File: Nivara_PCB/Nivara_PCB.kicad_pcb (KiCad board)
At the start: 2 copper layers, 102.2 x 83 mm, 58 parts, among them J1 NPN_IN, J10 Analog_Out, J11 RELAY, J2 PNP_IN, J3 D_IN, J4 Analaog_In, J5 RUN/STOP, J6 FUENTE, J7 NPN_OUT, J8 PNP_OUT, J9 RS485, Q1 IRLML6344, Q2 IRLML6344, Q3 IRLML6402, Q4 IRLML6402, U1 ESP32-S3-WROOM-1, U2 AP63203WU, U3 AP63205WU

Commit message: Cambios en el RS485
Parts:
- moved U1 17.7 mm to (194.1, 102.8)
- moved R5 9.10 mm to (155.7, 68.4), turned to 90 degrees
- renumbered TP4 to TP2, TP2 to TP3, TP3 to TP4
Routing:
- net /NIVARA_BOARD/NPN_IN/ESP_NPN_IN_1: track 8.14 -> 2.72 mm
- net +3.3V: track 82.8 -> 80.6 mm, vias 2 -> 4
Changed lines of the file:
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@@
 		(descr "SMD rectangular pad as test Point, square 1.0mm side length")
 		(tags "test point SMD pad rectangle square")
-		(property "Reference" "TP3"
+		(property "Reference" "TP4"
 			(at 0 -1.448 0)
 			(layer "F.SilkS")
@@
 	(footprint "RF_Module:ESP32-S3-WROOM-1"
 		(layer "F.Cu")
-		(at 184.7 87.75 -90)
+		(at 194.1 102.8 -90)
 		(descr "2.4 GHz Wi-Fi and Bluetooth module  https://www.espressif.com/sites/default/files/documentation/esp32-s3-wroom-1_wroom-1u_datasheet_en.pdf")
 		(tags "2.4 GHz Wi-Fi and Bluetooth module")
@@
 			(polygon
 				(pts
-					(xy 191.45 63.75) (xy 191.45 111.75) (xy 212.45 111.75) (xy 212.45 63.75)
+					(xy 200.85 78.8) (xy 200.85 126.8) (xy 221.85 126.8) (xy 221.85 78.8)
 				)
 			)
@@
 		(descr "SMD rectangular pad as test Point, square 1.0mm side length")
 		(tags "test point SMD pad rectangle square")
-		(property "Reference" "TP4"
+		(property "Reference" "TP2"
 			(at 0 -1.448 0)
 			(layer "F.SilkS")
@@
 		(descr "SMD rectangular pad as test Point, square 1.0mm side length")
 		(tags "test point SMD pad rectangle square")
-		(property "Reference" "TP2"
+		(property "Reference" "TP3"
 			(at 2.5 -0.1 0)
 			(layer "F.SilkS")
@@
 	(footprint "PCM_Resistor_SMD_AKL:R_0603_1608Metric"
 		(layer "F.Cu")
-		(at 164.7 69.7)
+		(at 155.7 68.375 90)
 		(descr "Resistor SMD 0603 (1608 Metric), square (rectangular) end terminal, IPC_7351 nominal, (Body size source: IPC-SM-782 page 72, https://www.pcb-3d.com/wordpress/wp-content/uploads/ipc-sm-782a_amendment_1_and_2.pdf), Alternate KiCad Library")
 		(tags "resistor")
 		(property "Reference" "R5"
-			(at -3.175 0 0)
+			(at -3.175 0 90)
 			(layer "F.SilkS")
 			(effects
@@
 		)
 		(property "Value" "10k"
-			(at 0 1.43 0)
+			(at 0 1.43 90)
 			(layer "F.Fab")
 			(hide yes)
@@
 		)
 		(property "Datasheet" ""
-			(at 0 0 0)
+			(at 0 0 90)
 			(layer "F.Fab")
 			(hide yes)
@@
 		)
 		(property "Description" "SMD 0603 Chip Resistor, US Symbol, Alternate KiCad Library"
-			(at 0 0 0)
+			(at 0 0 90)
 			(layer "F.Fab")
 			(hide yes)
@@
 		(attr smd)
 		(fp_line
-			(start -1.5 -0.8)
-			(end -1.5 0.8)
+			(start 1.5 -0.8)
+			(end -1.5 -0.8)
 			(stroke
 				(width 0.12)
@@
 		)
 		(fp_line
-			(start -1.5 0.8)
-			(end 1.5 0.8)
+			(start -1.5 -0.8)
+			(end -1.5 0.8)
 			(stroke
 				(width 0.12)
@@
 		)
 		(fp_line
-			(start 1.5 -0.8)
-			(end -1.5 -0.8)
+			(start 1.5 0.8)
+			(end 1.5 -0.8)
 			(stroke
 				(width 0.12)
@@
 		)
 		(fp_line
-			(start 1.5 0.8)
-			(end 1.5 -0.8)
+			(start -1.5 0.8)
+			(end 1.5 0.8)
 			(stroke
 				(width 0.12)
@@
 		)
 		(fp_line
-			(start -1.48 -0.73)
-			(end 1.48 -0.73)
+			(start 1.48 -0.73)
+			(end 1.48 0.73)
 			(stroke
 				(width 0.05)
@@
 		)
 		(fp_line
-			(start -1.48 0.73)
-			(end -1.48 -0.73)
+			(start -1.48 -0.73)
+			(end 1.48 -0.73)
 			(stroke
 				(width 0.05)
@@
 		)
 		(fp_line
-			(start 1.48 -0.73)
-			(end 1.48 0.73)
+			(start 1.48 0.73)
+			(end -1.48 0.73)
 			(stroke
 				(width 0.05)
@@
 		)
 		(fp_line
-			(start 1.48 0.73)
-			(end -1.48 0.73)
+			(start -1.48 0.73)
+			(end -1.48 -0.73)
 			(stroke
 				(width 0.05)
@@
 		)
 		(fp_line
-			(start -0.8 -0.4125)
-			(end 0.8 -0.4125)
+			(start 0.8 -0.4125)
+			(end 0.8 0.4125)
 			(stroke
 				(width 0.1)
@@
 		)
 		(fp_line
-			(start -0.8 0.4125)
-			(end -0.8 -0.4125)
+			(start -0.8 -0.4125)
+			(end 0.8 -0.4125)
 			(stroke
 				(width 0.1)
@@
 		)
 		(fp_line
-			(start 0.8 -0.4125)
-			(end 0.8 0.4125)
+			(start 0.8 0.4125)
+			(end -0.8 0.4125)
 			(stroke
 				(width 0.1)
@@
 		)
 		(fp_line
-			(start 0.8 0.4125)
-			(end -0.8 0.4125)
+			(start -0.8 0.4125)
+			(end -0.8 -0.4125)
 			(stroke
 				(width 0.1)
@@
 		)
 		(fp_text user "${REFERENCE}"
-			(at 0 0 0)
+			(at 0 0 90)
 			(layer "F.Fab")
 			(effects
@@
 		)
 		(pad "1" smd roundrect
-			(at -0.825 0)
+			(at -0.825 0 90)
 			(size 0.8 0.95)
 			(layers "F.Cu" "F.Mask" "F.Paste")
@@
 		)
 		(pad "2" smd roundrect
-			(at 0.825 0)
+			(at 0.825 0 90)
 			(size 0.8 0.95)
 			(layers "F.Cu" "F.Mask" "F.Paste")
@@
 	)
 	(segment
-		(start 153.45 69.7)
+		(start 152.95 69.2)
 		(end 151.65 67.9)
 		(width 0.4)
@@
 	)
 	(segment
-		(start 108.2 64.05)
-		(end 107.1 62.95)
-		(width 0.6)
+		(start 155.7 69.2)
+		(end 152.95 69.2)
+		(width 0.4)
 		(layer "F.Cu")
 		(net 1)
 	)
 	(segment
-		(start 169.2 68)
-		(end 169.2 67.525)
-		(width 0.4)
+		(start 108.2 64.05)
+		(end 107.1 62.95)
+		(width 0.6)
 		(layer "F.Cu")
 		(net 1)
@@
 	)
 	(segment
-		(start 163.875 69.7)
-		(end 153.45 69.7)
-		(width 0.4)
-		(layer "F.Cu")
-		(net 1)
-	)
-	(segment
 		(start 108.2 64.95)
 		(end 108.2 64.05)
@@
 	)
 	(segment
-		(start 166.1 71.1)
-		(end 169.2 68)
-		(width 0.4)
-		(layer "F.Cu")
-		(net 1)
-	)
-	(segment
 		(start 106.15 64.95)
 		(end 110.5 64.95)
@@
 	)
 	(segment
-		(start 164.6 71.1)
-		(end 166.1 71.1)
-		(width 0.4)
-		(layer "F.Cu")
-		(net 1)
-	)
-	(segment
-		(start 163.875 70.375)
-		(end 164.6 71.1)
-		(width 0.4)
-		(layer "F.Cu")
-		(net 1)
-	)
-	(segment
 		(start 105.9 72.1)
 		(end 106.05 71.95)
@@
 		(net 1)
 	)
-	(segment
-		(start 163.875 69.7)
-		(end 163.875 70.375)
-		(width 0.4)
-		(layer "F.Cu")
-		(net 1)
-	)
 	(via
 		(at 149.825 67.9)
@@
 		(net 1)
 	)
+	(via
+		(at 169.2 67.525)
+		(size 0.6)
+		(drill 0.3)
+		(layers "F.Cu" "B.Cu")
+		(net 1)
+	)
+	(via
+		(at 155.7 69.2)
+		(size 0.6)
+		(drill 0.3)
+		(layers "F.Cu" "B.Cu")
+		(net 1)
+	)
 	(segment
 		(start 140.2 67.9)
@@
 	)
 	(segment
+		(start 167.525 69.2)
+		(end 169.2 67.525)
+		(width 0.4)
+		(layer "B.Cu")
+		(net 1)
+	)
+	(segment
+		(start 155.7 69.2)
+		(end 167.525 69.2)
+		(width 0.4)
+		(layer "B.Cu")
+		(net 1)
+	)
+	(segment
 		(start 149.825 67.9)
 		(end 140.2 67.9)
@@
 	)
 	(via
-		(at 166.1 68.4)
+		(at 166.9 67.8)
 		(size 0.6)
 		(drill 0.3)
@@
 	)
 	(segment
-		(start 164.225 68.4)
-		(end 159.38 68.4)
-		(width 0.4)
-		(layer "F.Cu")
-		(net 74)
-	)
-	(segment
-		(start 165.525 69.7)
-		(end 164.225 68.4)
+		(start 158.17 67.55)
+		(end 158.35 67.37)
 		(width 0.4)
 		(layer "F.Cu")
@@
 	)
 	(segment
-		(start 159.38 68.4)
-		(end 158.35 67.37)
+		(start 155.7 67.55)
+		(end 158.17 67.55)
 		(width 0.4)
 		(layer "F.Cu")

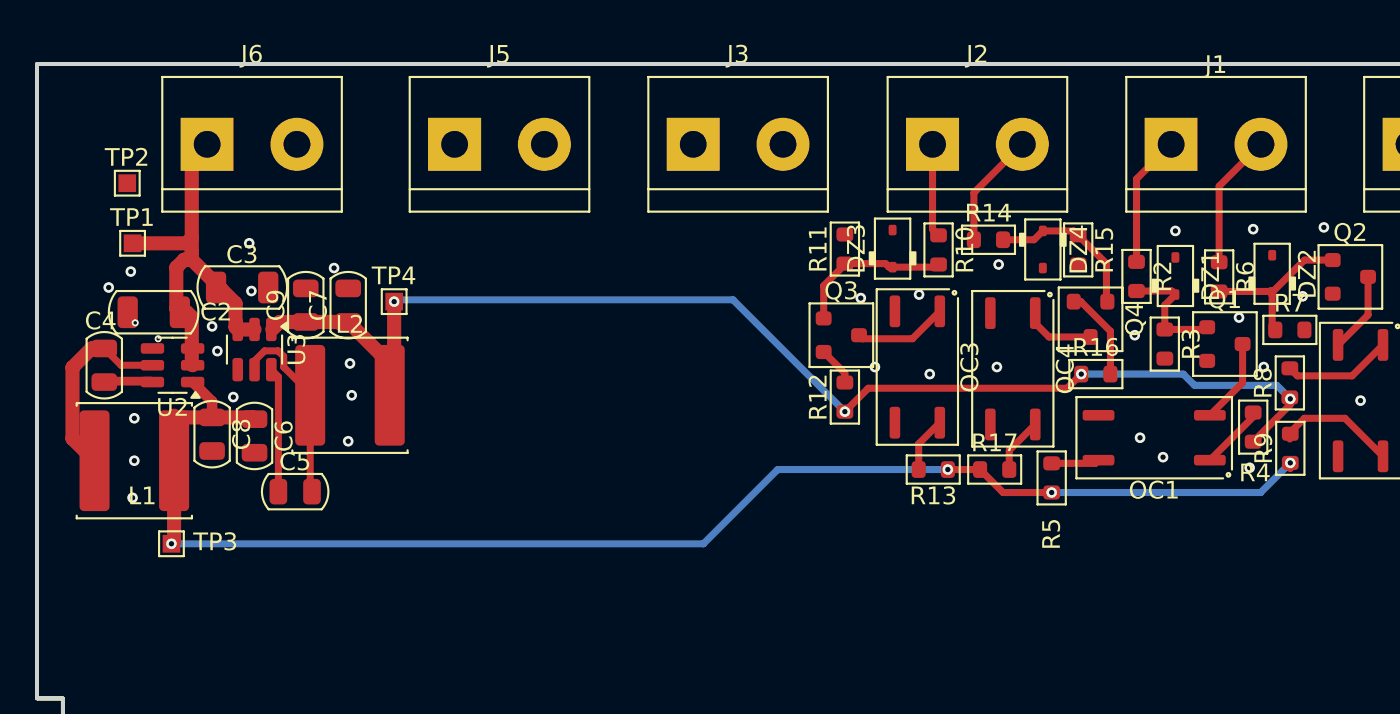
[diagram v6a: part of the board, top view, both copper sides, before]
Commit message: Añadido de diodo TVS y resetteable fuse.
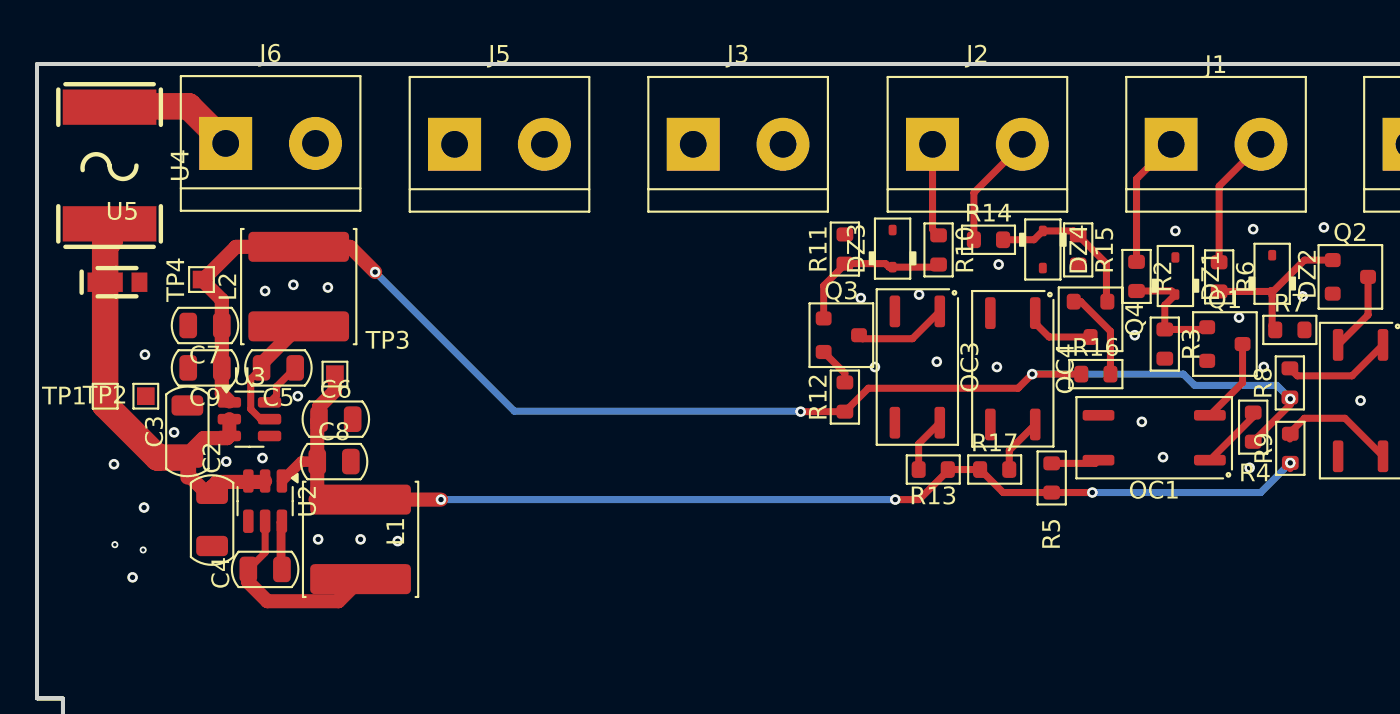
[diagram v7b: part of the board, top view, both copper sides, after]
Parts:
- added U4: 2920L185DR, Fuse_Holder:F2920, F.Cu at (102.4, 50.7)
- added U5: CUHZ30V,H3F, Fuse_Holder:SOD-323HE_L2.0-W1.4-LS2.5-RD, F.Cu at (103.1, 57.3)
- moved C4 14.7 mm to (111.2, 73.5), turned to 180 degrees
- moved L1 13.6 mm to (116.6, 71.8), turned to 90 degrees
- moved TP3 13.3 mm to (115.2, 62.5), turned to 90 degrees
- moved C2 12.2 mm to (108.2, 70.8), turned to -90 degrees
- moved TP2 12.1 mm to (104.5, 63.8), turned to 90 degrees
- moved TP4 11.0 mm to (107.6, 57.1), turned to 90 degrees
- moved U2 9.30 mm to (111.2, 69.7), turned to -90 degrees
- moved TP1 8.79 mm to (102.2, 63.8), turned to 90 degrees
- moved C3 8.72 mm to (106.8, 65.8), turned to 90 degrees
- moved C7 8.18 mm to (107.8, 59.8), turned to 180 degrees
- moved C8 7.07 mm to (115.1, 67.5), turned to 0 degrees
- moved C5 7.06 mm to (112.0, 62.1), turned to 180 degrees
- moved L2 6.80 mm to (113.1, 57.5), turned to 90 degrees
- moved C9 6.72 mm to (107.8, 62.1), turned to 180 degrees
- moved C6 4.70 mm to (115.2, 65.0), turned to 0 degrees
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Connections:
- J6 pad 1: VCC -> Net-(J6-Pin_1)
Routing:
- net +3.3V: track 80.6 -> 67.1 mm
- net +5V: track 73.1 -> 81.3 mm
- net Net-(J6-Pin_1): track 0.00 -> 7.46 mm
- net Net-(U3-BST): track 7.07 -> 2.55 mm
- net VCC: track 23.5 -> 27.6 mm
- net Net-(U3-SW): track 10.8 -> 7.10 mm

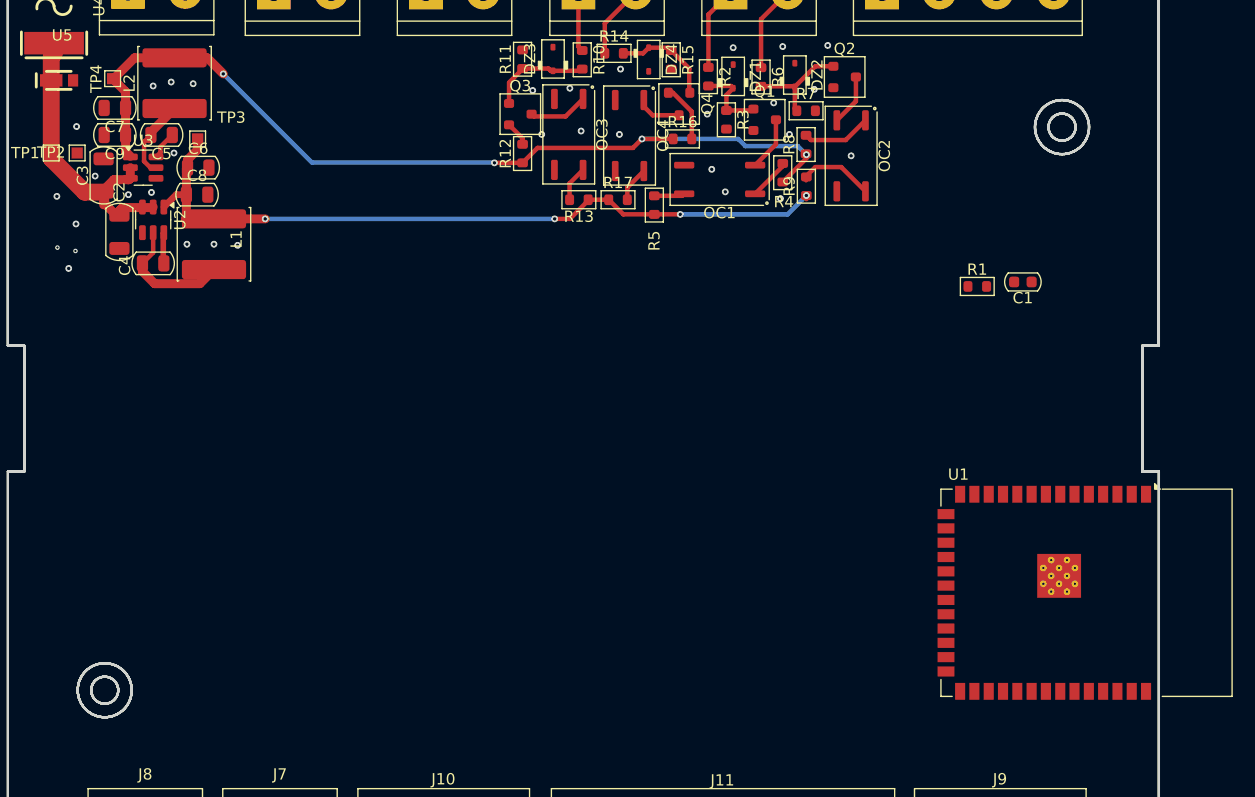
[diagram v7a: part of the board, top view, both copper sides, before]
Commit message: Ajuste de RS-485 y protección de alimentación contra cortocircuito y sobre voltaje.
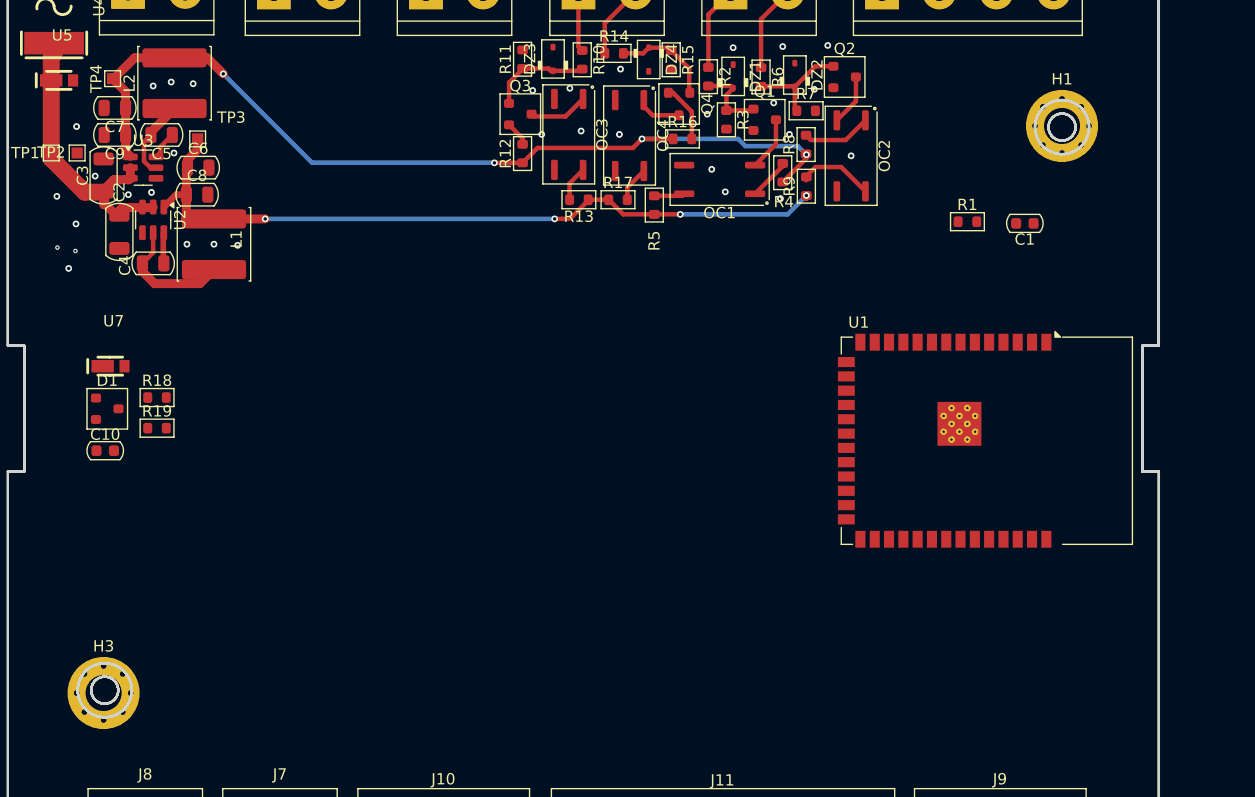
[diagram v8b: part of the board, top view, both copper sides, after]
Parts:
- added C10: 1uF, PCM_Capacitor_SMD_AKL:C_0603_1608Metric, F.Cu at (106.9, 90.2)
- added D1: SM712, PCM_Package_TO_SOT_SMD_AKL:SOT-23, F.Cu at (107.1, 86.5)
- added H1: MountingHole_Pad, MountingHole:MountingHole_3.2mm_M3_Pad_Via, F.Cu at (191.9, 61.4)
- added H3: MountingHole_Pad, MountingHole:MountingHole_3.2mm_M3_Pad_Via, F.Cu at (106.8, 111.7)
- added R18: R_0603, PCM_Resistor_SMD_AKL:R_0603_1608Metric, F.Cu at (111.5, 85.5)
- added R19: R_0603, PCM_Resistor_SMD_AKL:R_0603_1608Metric, F.Cu at (111.5, 88.2)
- added U7: CUHZ30V,H3F, Fuse_Holder:SOD-323HE_L2.0-W1.4-LS2.5-RD, F.Cu at (107.7, 82.7)
- moved U1 16.1 mm to (185.2, 89.3)
- moved R1 5.82 mm to (183.5, 69.8)
- moved C1 5.20 mm to (188.6, 70.0)
